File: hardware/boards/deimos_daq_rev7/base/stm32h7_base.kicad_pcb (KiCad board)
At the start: 4 copper layers, 196 parts, among them IC1 STM32H743ZIT6, IC10001 TPS560430XDBVR, IC10002 TPS560430XDBVR, IC4001 TPS560430XDBVR, IC5004 REF35102QDBVR, IC8001 INA826AIDR, J3001 RCH_RC01133, J4 Conn_02x07_Odd_Even, J8001 Barrel_Jack PJ-202BH, T1 H1102NLT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

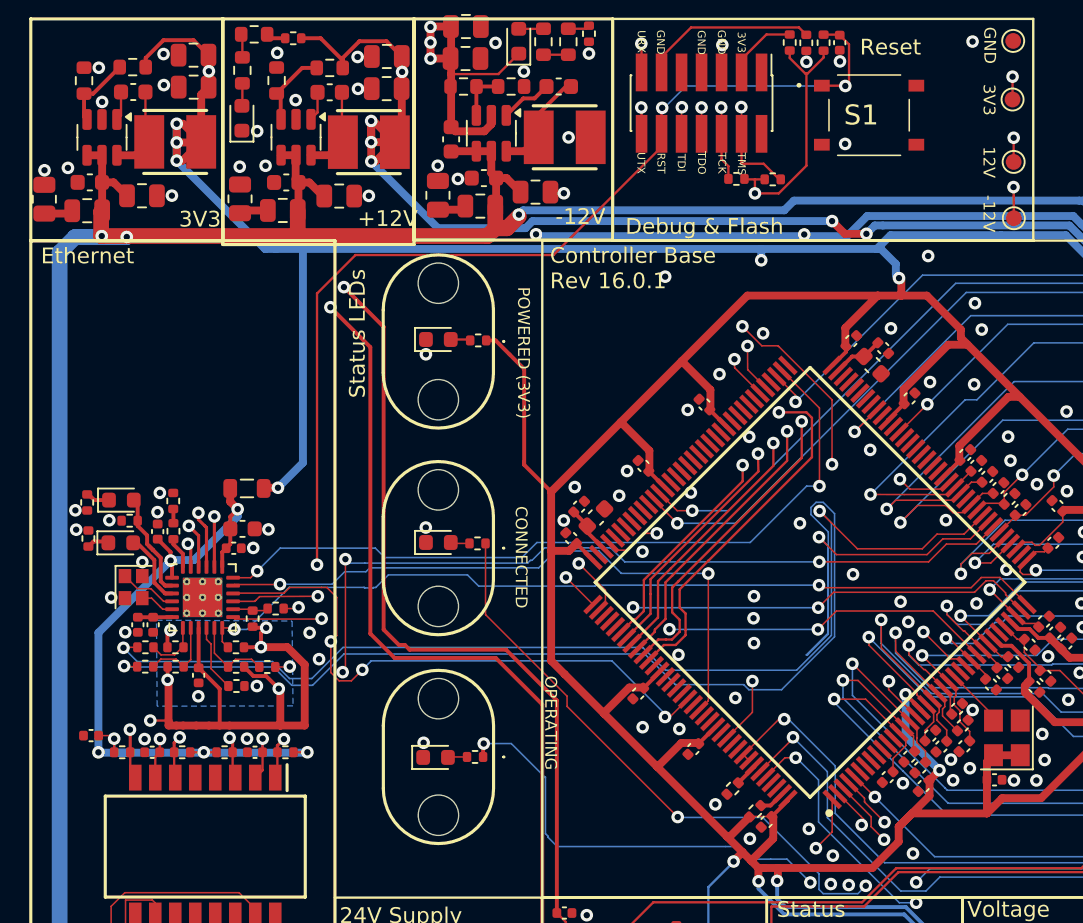
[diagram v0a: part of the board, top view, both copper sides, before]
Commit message: DNP light pipes. move rmii traces to in2.
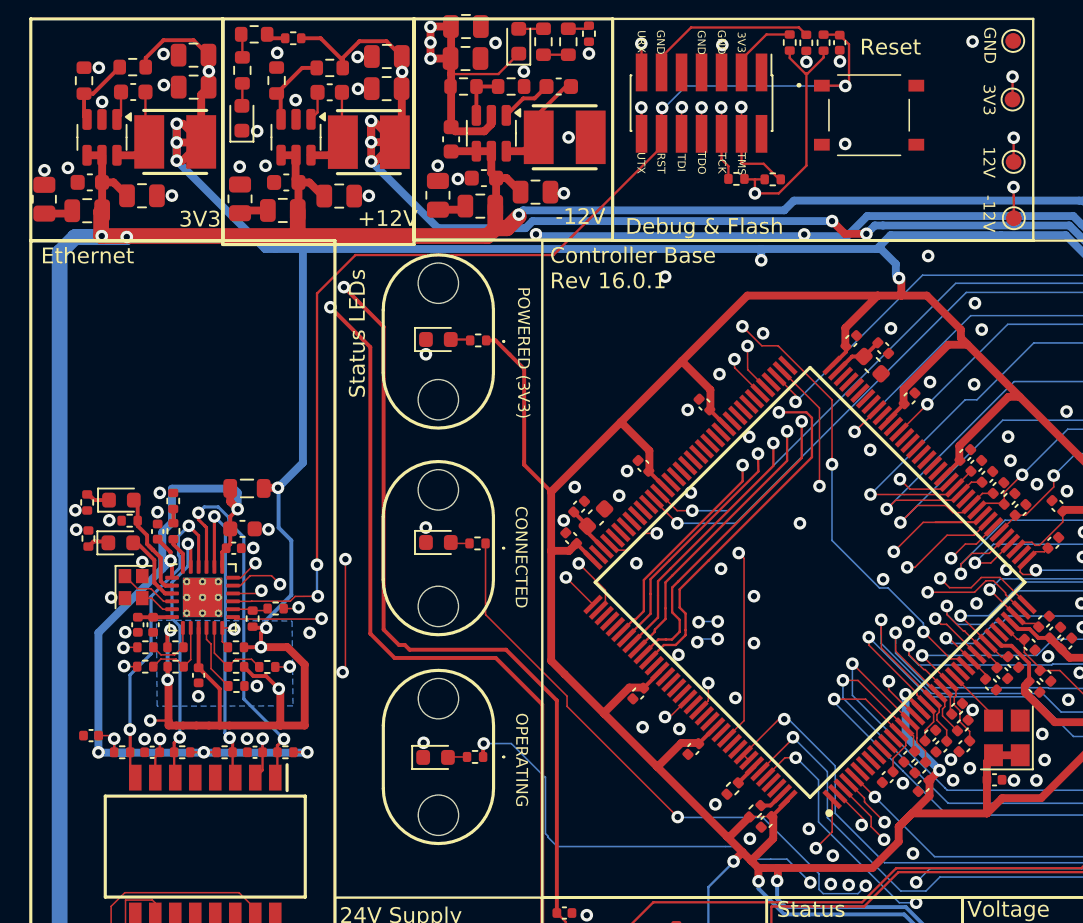
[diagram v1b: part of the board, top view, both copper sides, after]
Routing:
- net /Micro/RMII_RXD0: track 90.2 -> 64.3 mm
- net /Micro/RMII_TXD0: track 46.5 -> 39.4 mm, vias 3 -> 2
- net /Micro/RMII_MDIO: track 55.4 -> 61.6 mm
- net Net-(T1-CT_1): track 55.1 -> 59.9 mm
- net /Micro/RMII_MDC: track 49.6 -> 53.5 mm, vias 3 -> 4
- net /Micro/RMII_CRS_DV: track 54.7 -> 57.6 mm
- net /Micro/RMII_RXD1: track 69.5 -> 66.6 mm
- net /Micro/RMII_REF_CLK: track 50.1 -> 52.1 mm, vias 3 -> 4
- net /Micro/RMII_TXD1: track 48.5 -> 50.4 mm
- net /Micro/DEBUG_TDI: track 60.8 -> 59.3 mm
- net /Micro/RMII_TX_EN: track 37.3 -> 35.8 mm, vias 3 -> 2
- net +3V3: track 503.6 -> 504.4 mm
- net /Micro/Ethernet/RX-: track 21.2 -> 20.6 mm
- net GND: vias 128 -> 126

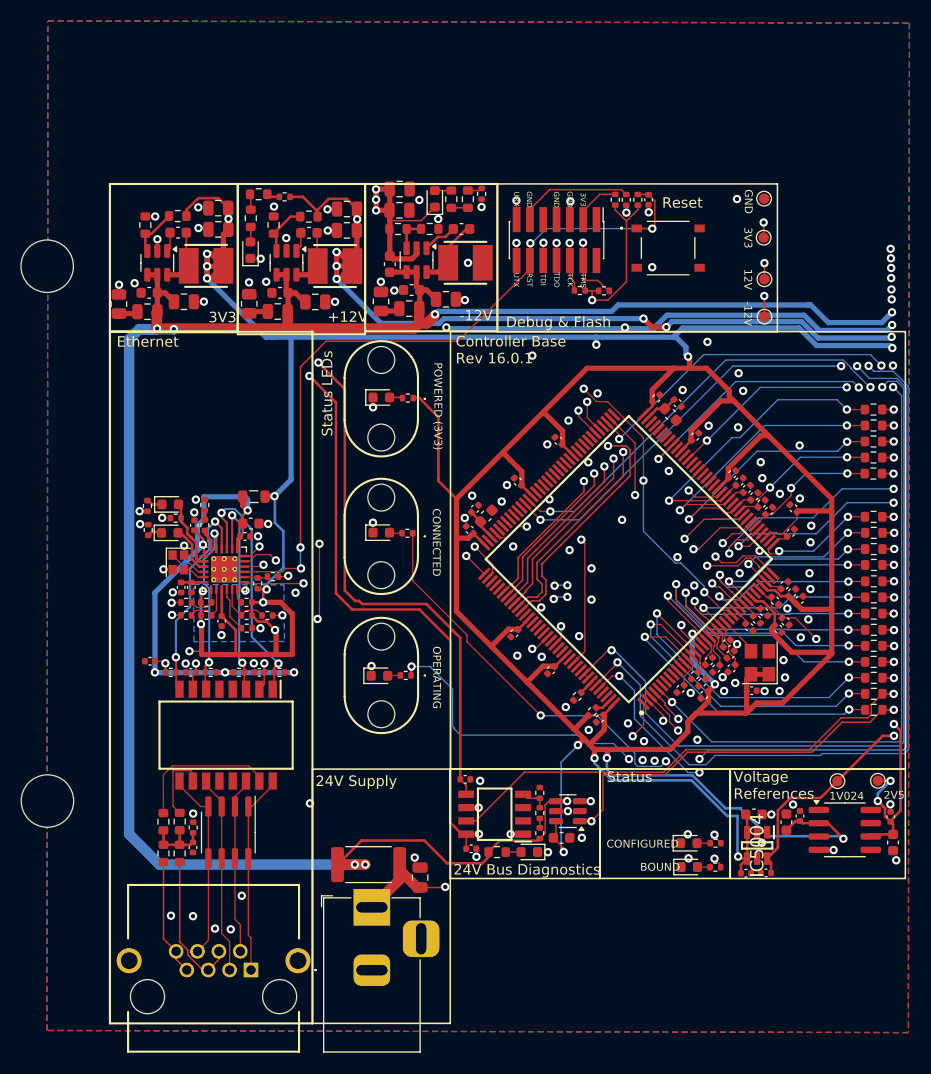
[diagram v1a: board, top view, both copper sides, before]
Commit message: better routing for ethernet
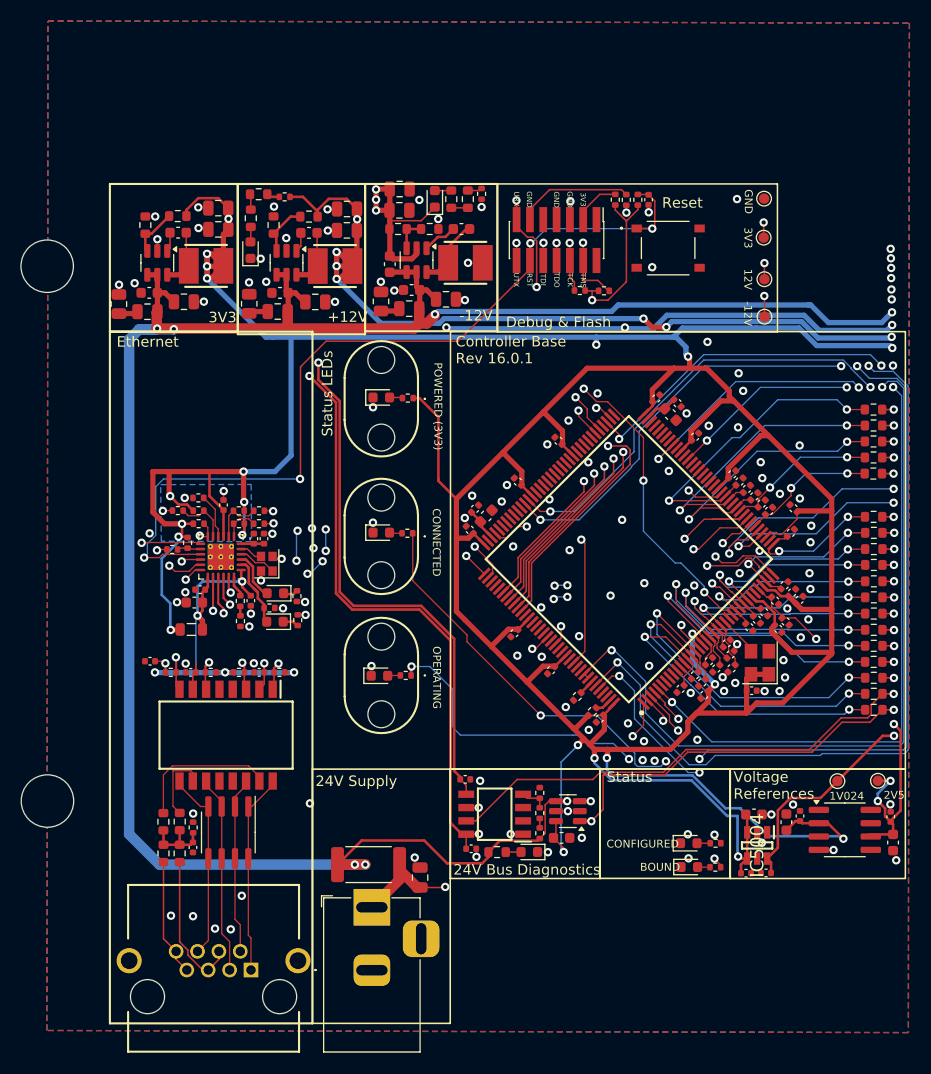
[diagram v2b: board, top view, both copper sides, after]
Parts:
- moved R34 18.0 mm to (58.8, 112.1), turned to -90 degrees
- moved R31 15.5 mm to (58.7, 109.8), turned to -90 degrees
- moved D36 15.0 mm to (56.6, 112.3), turned to 180 degrees
- moved FB1 14.0 mm to (48.6, 113.0), turned to 0 degrees
- moved R30 13.3 mm to (49.3, 100.5), turned to 0 degrees
- moved R47 13.2 mm to (47.3, 101.7), turned to 0 degrees
- moved R33 12.4 mm to (56.1, 111.0), turned to 0 degrees
- moved R26 12.2 mm to (55.1, 101.7), turned to 0 degrees
- moved D2 11.6 mm to (56.6, 109.6), turned to 180 degrees
- moved R57 11.6 mm to (53.3, 112.2), turned to 90 degrees
- moved C26 11.1 mm to (51.7, 101.2), turned to -90 degrees
- moved R28 11.0 mm to (49.3, 101.7), turned to 0 degrees
- moved R49 10.4 mm to (53.1, 101.7), turned to 180 degrees
- moved R23 10.2 mm to (55.1, 102.9), turned to 0 degrees
- moved R48 9.95 mm to (46.8, 105.4), turned to 180 degrees
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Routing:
- net /Micro/RMII_MDC: track 53.5 -> 73.6 mm
- net /Micro/RMII_TXD0: track 39.4 -> 54.8 mm, vias 2 -> 4
- net /Micro/RMII_REF_CLK: track 52.1 -> 67.4 mm
- net /Micro/RMII_TXD1: track 50.4 -> 64.4 mm, vias 2 -> 4
- net /Micro/DEBUG_RESET: track 116.5 -> 129.7 mm
- net Net-(T1-CT_1): track 59.9 -> 47.1 mm, vias 8 -> 7
- net /Micro/RMII_RXD1: track 66.6 -> 54.4 mm, vias 2 -> 4
- net /Micro/RMII_RXD0: track 64.3 -> 52.7 mm, vias 2 -> 4
- net /Micro/RMII_TX_EN: track 35.8 -> 45.8 mm
- net /Micro/Ethernet/TX+: track 24.2 -> 15.6 mm
- net /Micro/Ethernet/TX-: track 20.4 -> 12.0 mm
- net /Micro/DEBUG_TDI: track 59.3 -> 53.1 mm
- net /Micro/DEBUG_TDO/SWO: track 57.3 -> 51.6 mm
- net /Micro/DEBUG_TCK/SWCLK: track 60.8 -> 55.1 mm
- net /Micro/DEBUG_TMS/SWDIO: track 58.4 -> 53.0 mm
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
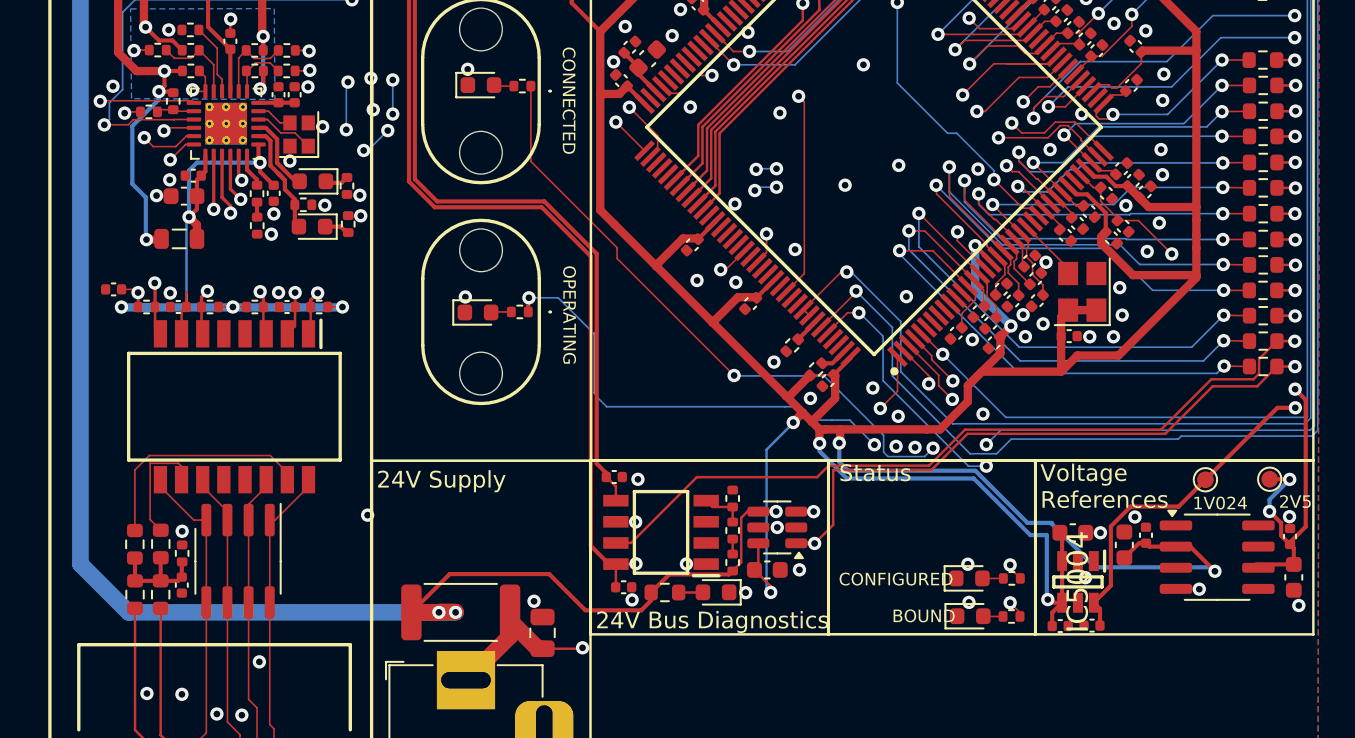
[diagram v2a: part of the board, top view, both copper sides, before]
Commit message: improve routing of ethernet traces, ADC input traces, and grounding for ADC input caps
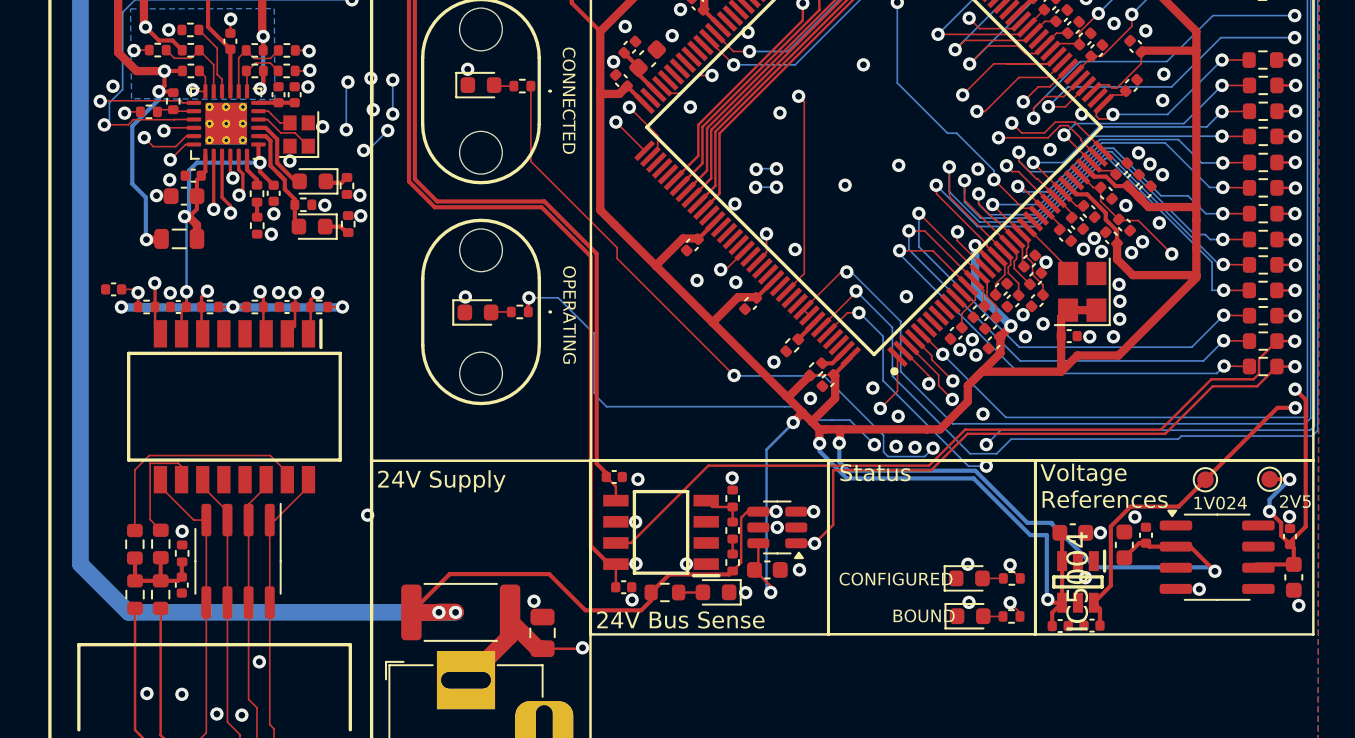
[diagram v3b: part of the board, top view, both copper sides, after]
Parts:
- moved C28 0.11 mm to (105.4, 112.2)
- turned C32 to -45 degrees
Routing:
- net /Micro/AIN3_Filt: track 30.0 -> 34.3 mm
- net /Micro/Ethernet/RX-: track 18.5 -> 14.9 mm
- net /Micro/AIN4_Filt: track 30.9 -> 34.3 mm
- net /Micro/AIN5_Filt: track 27.3 -> 30.6 mm
- net /Micro/AIN6_Filt: track 22.7 -> 26.0 mm
- net /Micro/AIN7_Filt: track 22.7 -> 25.0 mm
- net /Micro/Ethernet/RX+: track 14.4 -> 12.9 mm
- net /Micro/AIN8_Filt: track 18.6 -> 19.7 mm
- net /Micro/Ethernet/TX+: track 15.6 -> 14.9 mm
- net Net-(T1-CT_1): vias 7 -> 8
- net GND: vias 125 -> 134
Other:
- board text added: "24V Bus Sense"
- board text removed: "24V Bus Diagnostics"
